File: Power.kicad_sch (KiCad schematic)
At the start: 106 parts, among them Y1 16M

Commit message: Ревью rev0.1-plus4, раунд 3 (11 силовик, 13 ЭМС): C134 100n 100V у J6 на B.Cu; C37/C39/C64 15n; R50 DNP; вывод 4 U4/U9/U12 на GND (под INA241A2); cflow исправлен — стакан связан с медью у стенки, сетка 0.05 мм, меры у шунта вместо пика (медь узла была занижена в 1.3–2.4 раза, решения в силе, фазы по меди равны 0.52–0.58 мОм); ответы 12/14; DRC 0/0/0
Co-Authored-By: Claude Opus 5.5 <noreply@anthropic.com>
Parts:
- added C134: 100n 100V X7R, Capacitor_SMD:C_0805_2012Metric_Pad1.18x1.45mm_HandSolder, symbol Device:C_Small
- R50: now not fitted
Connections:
- net GND: now also C134.2
- net VDC: now also C134.1
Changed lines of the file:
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@@
 	(symbol
 		(lib_id "Device:C_Small")
+		(at 304.8 210.82 0)
+		(unit 1)
+		(body_style 1)
+		(exclude_from_sim no)
+		(in_bom yes)
+		(on_board yes)
+		(in_pos_files yes)
+		(dnp no)
+		(property "Reference" "C134"
+			(at 307.34 210.185 0)
+			(show_name no)
+			(do_not_autoplace no)
+			(effects
+				(font
+					(size 1.27 1.27)
+				)
+				(justify left)
+			)
+		)
+		(property "Value" "100n 100V X7R"
+			(at 307.34 212.725 0)
+			(show_name no)
+			(do_not_autoplace no)
+			(effects
+				(font
+					(size 1.27 1.27)
+				)
+				(justify left)
+			)
+		)
+		(property "Footprint" "Capacitor_SMD:C_0805_2012Metric_Pad1.18x1.45mm_HandSolder"
+			(at 304.8 210.82 0)
+			(hide yes)
+			(show_name no)
+			(do_not_autoplace no)
+			(effects
+				(font
+					(size 1.27 1.27)
+				)
+			)
+		)
+		(property "Datasheet" ""
+			(at 304.8 210.82 0)
+			(hide yes)
+			(show_name no)
+			(do_not_autoplace no)
+			(effects
+				(font
+					(size 1.27 1.27)
+				)
+			)
+		)
+		(property "Description" ""
+			(at 304.8 210.82 0)
+			(hide yes)
+			(show_name no)
+			(do_not_autoplace no)
+			(effects
+				(font
+					(size 1.27 1.27)
+				)
+			)
+		)
+		(property "Description P/N" "Capacitor SMD 100V X7R"
+			(at 304.8 210.82 0)
+			(hide yes)
+			(show_name no)
+			(do_not_autoplace no)
+			(effects
+				(font
+					(size 1.27 1.27)
+				)
+			)
+		)
+		(pin "1"
+		)
+		(pin "2"
+		)
+		(instances
+			(project "Power"
+				(path "/7ff38f8b-11c9-43a1-8b76-b5e8c8de18e0"
+					(reference "C134")
+					(unit 1)
+				)
+			)
+		)
+	)
+	(symbol
+		(lib_id "power:VDC")
+		(at 304.8 208.28 0)
+		(unit 1)
+		(body_style 1)
+		(exclude_from_sim no)
+		(in_bom yes)
+		(on_board yes)
+		(in_pos_files yes)
+		(dnp no)
+		(property "Reference" "#PWR221"
+			(at 304.8 204.47 0)
+			(hide yes)
+			(show_name no)
+			(do_not_autoplace no)
+			(effects
+				(font
+					(size 1.27 1.27)
+				)
+			)
+		)
+		(property "Value" "VDC"
+			(at 304.8 204.47 0)
+			(show_name no)
+			(do_not_autoplace no)
+			(effects
+				(font
+					(size 1.27 1.27)
+				)
+			)
+		)
+		(property "Footprint" ""
+			(at 304.8 208.28 0)
+			(hide yes)
+			(show_name no)
+			(do_not_autoplace no)
+			(effects
+				(font
+					(size 1.27 1.27)
+				)
+			)
+		)
+		(property "Datasheet" ""
+			(at 304.8 208.28 0)
+			(hide yes)
+			(show_name no)
+			(do_not_autoplace no)
+			(effects
+				(font
+					(size 1.27 1.27)
+				)
+			)
+		)
+		(property "Description" ""
+			(at 304.8 208.28 0)
+			(hide yes)
+			(show_name no)
+			(do_not_autoplace no)
+			(effects
+				(font
+					(size 1.27 1.27)
+				)
+			)
+		)
+		(pin "1"
+		)
+		(instances
+			(project "Power"
+				(path "/7ff38f8b-11c9-43a1-8b76-b5e8c8de18e0"
+					(reference "#PWR221")
+					(unit 1)
+				)
+			)
+		)
+	)
+	(symbol
+		(lib_id "power:GND")
+		(at 304.8 213.36 0)
+		(unit 1)
+		(body_style 1)
+		(exclude_from_sim no)
+		(in_bom yes)
+		(on_board yes)
+		(in_pos_files yes)
+		(dnp no)
+		(property "Reference" "#PWR222"
+			(at 304.8 219.71 0)
+			(hide yes)
+			(show_name no)
+			(do_not_autoplace no)
+			(effects
+				(font
+					(size 1.27 1.27)
+				)
+			)
+		)
+		(property "Value" "GND"
+			(at 304.8 217.17 0)
+			(show_name no)
+			(do_not_autoplace no)
+			(effects
+				(font
+					(size 1.27 1.27)
+				)
+			)
+		)
+		(property "Footprint" ""
+			(at 304.8 213.36 0)
+			(hide yes)
+			(show_name no)
+			(do_not_autoplace no)
+			(effects
+				(font
+					(size 1.27 1.27)
+				)
+			)
+		)
+		(property "Datasheet" ""
+			(at 304.8 213.36 0)
+			(hide yes)
+			(show_name no)
+			(do_not_autoplace no)
+			(effects
+				(font
+					(size 1.27 1.27)
+				)
+			)
+		)
+		(property "Description" ""
+			(at 304.8 213.36 0)
+			(hide yes)
+			(show_name no)
+			(do_not_autoplace no)
+			(effects
+				(font
+					(size 1.27 1.27)
+				)
+			)
+		)
+		(pin "1"
+		)
+		(instances
+			(project "Power"
+				(path "/7ff38f8b-11c9-43a1-8b76-b5e8c8de18e0"
+					(reference "#PWR222")
+					(unit 1)
+				)
+			)
+		)
+	)
+	(symbol
+		(lib_id "Device:C_Small")
 		(at 448.31 222.25 0)
 		(unit 1)
@@
 		(on_board yes)
 		(in_pos_files yes)
-		(dnp no)
+		(dnp yes)
 		(property "Reference" "R50"
 			(at 597.916 317.754 0)

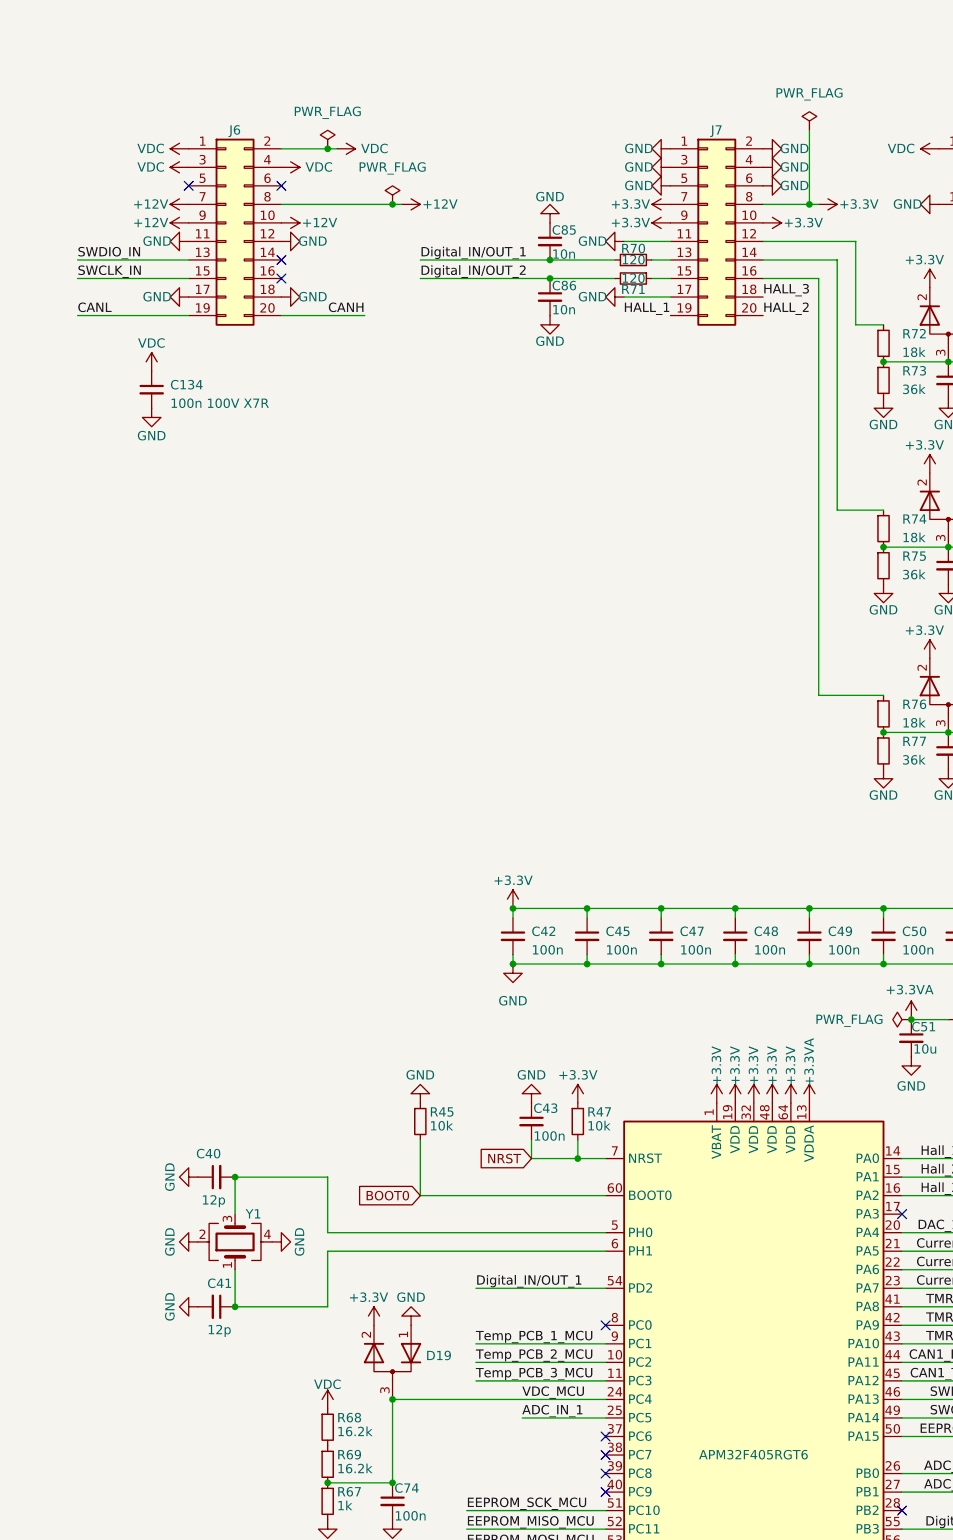
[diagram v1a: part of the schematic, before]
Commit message: Решения владельца после раунда 3: предохранитель F1 2410 на линии VDC к J6 (Bel 0679L1000, замена 0452001.MRL; J6, C134, R68 → /VDC_J6; VDC/GND C +0.6/+0.8 %); места под Y между J4/J5 — H5 CHASSIS (M3 с металлизацией), C135/C136 1812 DNP, зазор 2 мм (Power.kicad_dru); нормы ЭМС и решения по CAN и пазам в CHANGELOG; DRC 0/0/0
Co-Authored-By: Claude Opus 5.5 <noreply@anthropic.com>
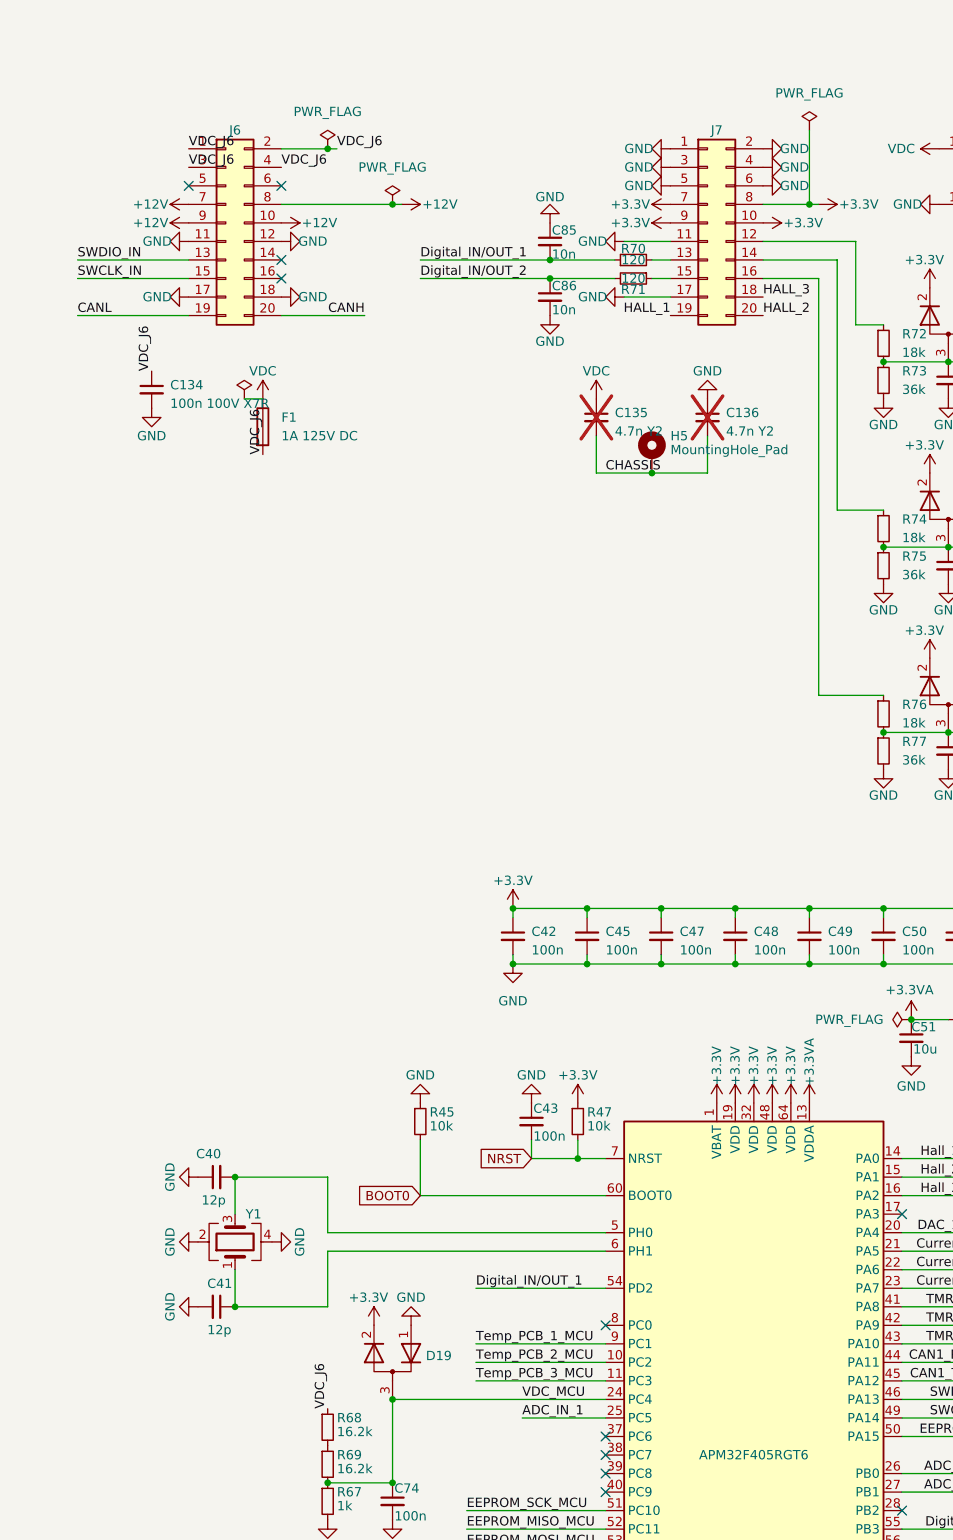
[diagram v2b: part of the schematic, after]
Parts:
- added C135, C136: 4.7n Y2, Capacitor_SMD:C_1812_4532Metric, symbol Device:C_Small
- added F1: 1A 125V DC, Fuse:Fuse_Littelfuse-NANO2-451_453, symbol Device:Fuse
- added H5: MountingHole_Pad, MountingHole:MountingHole_3.2mm_M3_Pad_Via, symbol Mechanical:MountingHole_Pad
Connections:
- net GND: now also C136.1
- net VDC: now also C135.1, F1.1; no longer C134.1, J6.1 (Pin_1), J6.2 (Pin_2), J6.3 (Pin_3), J6.4 (Pin_4), R68.1
- new net CHASSIS: C135.2, C136.2, H5.1
- new net VDC_J6: C134.1, F1.2, J6.1 (Pin_1), J6.2 (Pin_2), J6.3 (Pin_3), J6.4 (Pin_4), R68.1

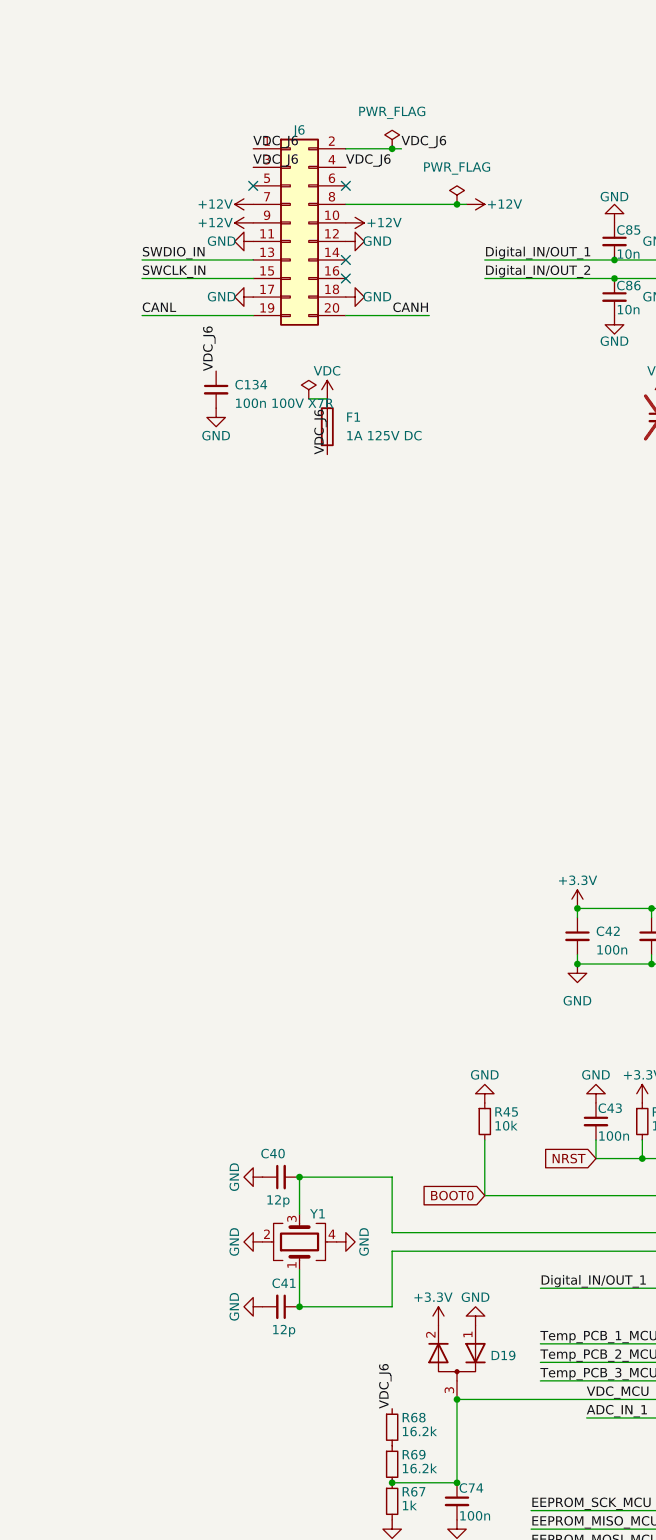
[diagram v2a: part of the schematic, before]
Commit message: Решения владельца: предохранитель снят с платы (на соединительную плату, плата и корневой лист — как в d30010b); снаббер R — 2 × 0805 1 Ом параллельно (R100–R105 + R124–R129) в пределах прежних пэдов 0612; места под Y между J4/J5 — H5 CHASSIS винтом в радиатор, C135/C136 DNP, зазор 2 мм; снабберы на части первых плат rev0.1; цель ЭМС — CISPR 25 класс 3; DRC 0/0/0
Co-Authored-By: Claude Opus 5.5 <noreply@anthropic.com>
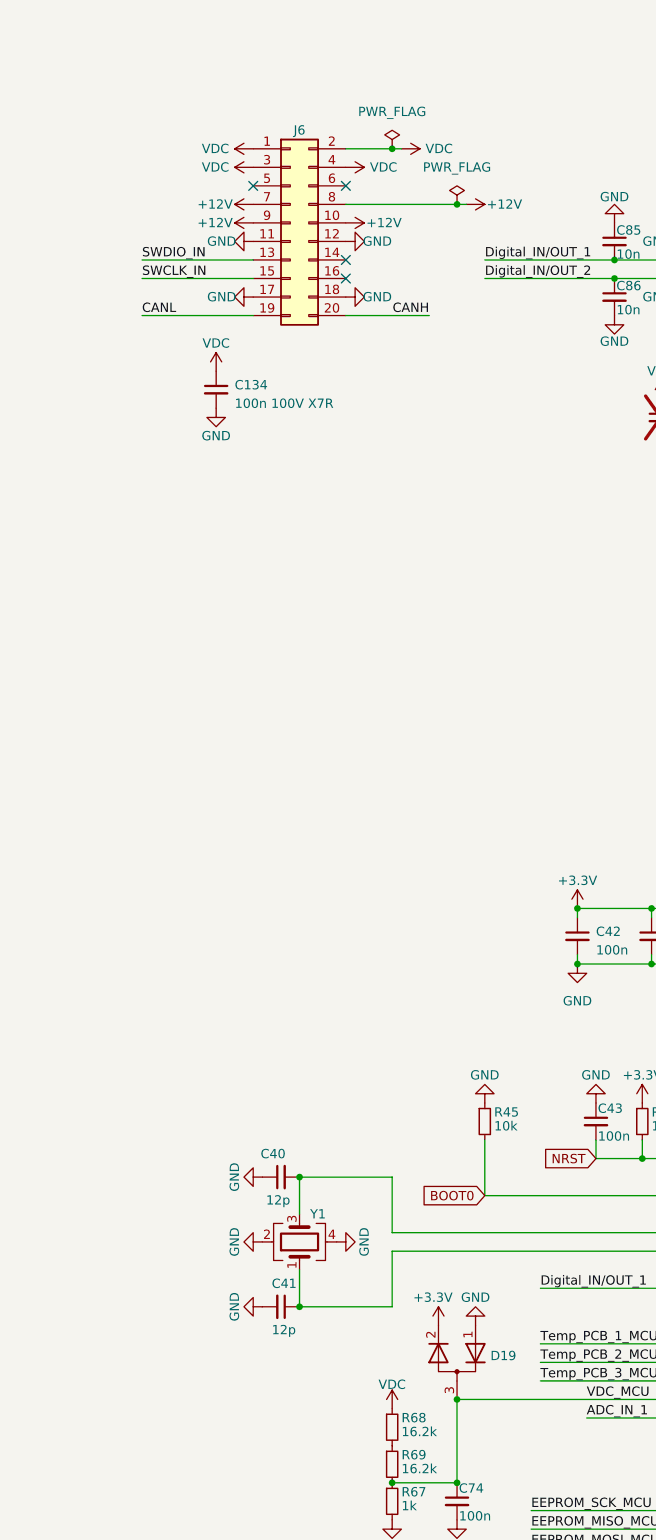
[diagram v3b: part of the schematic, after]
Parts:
- removed F1: 1A 125V DC, Fuse:Fuse_Littelfuse-NANO2-451_453, symbol Device:Fuse
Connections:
- net VDC_J6 is gone; now on net VDC: C134.1, J6.1 (Pin_1), J6.2 (Pin_2), J6.3 (Pin_3), J6.4 (Pin_4), R68.1
